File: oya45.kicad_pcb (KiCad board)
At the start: 2 copper layers, 190.5 x 95.2 mm, 94 parts, among them U1 ProMicro

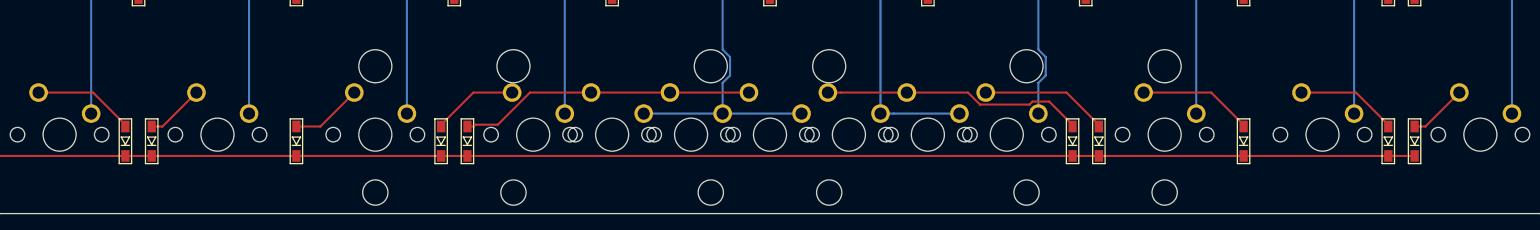
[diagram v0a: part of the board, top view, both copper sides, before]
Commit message: added bottom row footprints
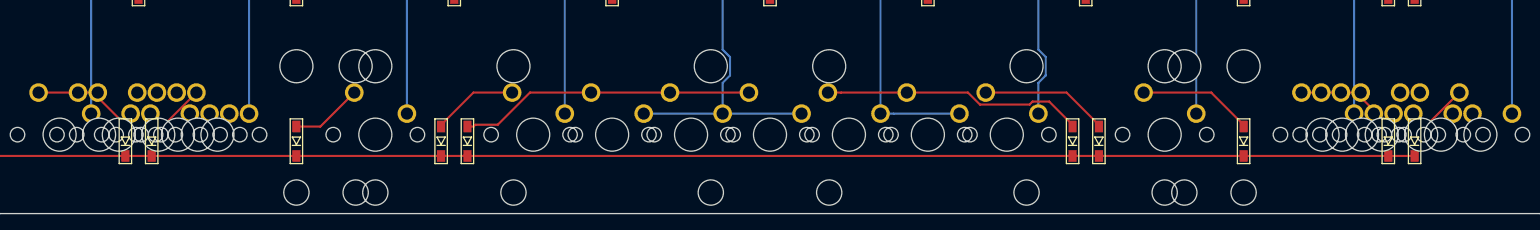
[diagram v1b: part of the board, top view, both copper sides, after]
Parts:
- added MX49: MX-NoLED, MX_Only:MXOnly-6.25U-ReversedStabilizers-NoSwitch, B.Cu at (142.9, 114.3)
- added MX50: MX-NoLED, MX_Only:MXOnly-7U-ReversedStabilizers-NoSwitch, B.Cu at (142.9, 114.3)
- added MX51: MX-NoLED, MX_Only:MXOnly-1.25U-NoLED, B.Cu at (73.8, 114.3)
- added MX52: MX-NoLED, MX_Only:MXOnly-1.25U-NoLED, B.Cu at (71.4, 114.3)
- added MX53: MX-NoLED, MX_Only:MXOnly-1.25U-NoLED, B.Cu at (64.3, 114.3)
- added MX54: MX-NoLED, MX_Only:MXOnly-1.5U-NoLED, B.Cu at (69.1, 114.3)
- added MX55: MX-NoLED, MX_Only:MXOnly-1.5U-NoLED, B.Cu at (61.9, 114.3)
- added MX57: MX-NoLED, MX_Only:MXOnly-1.25U-NoLED, B.Cu at (214.3, 114.3)
- added MX58: MX-NoLED, MX_Only:MXOnly-1.25U-NoLED, B.Cu at (211.9, 114.3)
- added MX59: MX-NoLED, MX_Only:MXOnly-1.25U-NoLED, B.Cu at (221.5, 114.3)
- added MX60: MX-NoLED, MX_Only:MXOnly-1.5U-NoLED, B.Cu at (216.7, 114.3)
- added MX61: MX-NoLED, MX_Only:MXOnly-1.5U-NoLED, B.Cu at (223.8, 114.3)

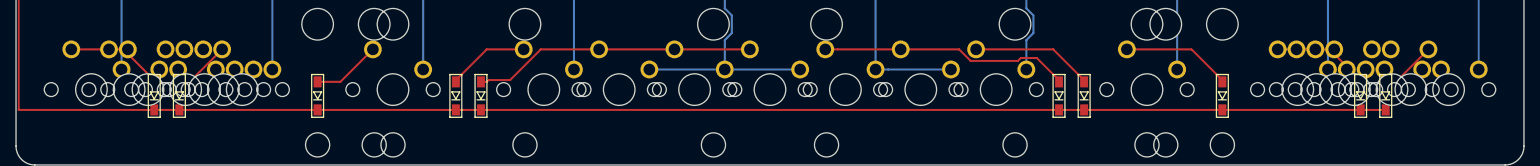
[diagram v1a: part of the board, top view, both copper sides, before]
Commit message: fixed diodes
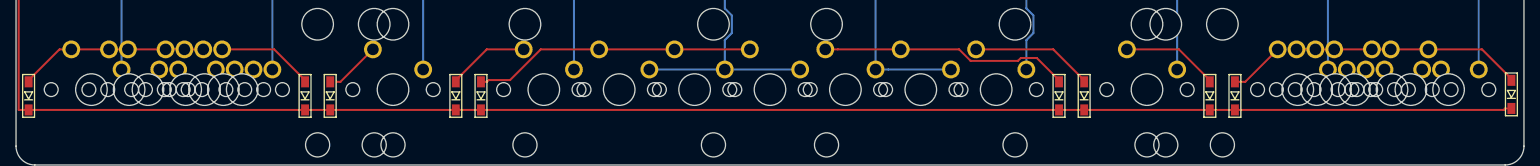
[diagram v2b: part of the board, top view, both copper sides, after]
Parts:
- moved D40 15.9 mm to (236.5, 114.9)
- moved D31 15.9 mm to (49.2, 115.1)
- moved D32 15.9 mm to (84.1, 115.1)
- moved D39 15.9 mm to (201.6, 115.1)
- moved D33 1.59 mm to (87.3, 115.1)
- moved D38 1.59 mm to (198.4, 115.1)
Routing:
- net Net-(D40-Pad2): track 7.10 -> 28.9 mm
- net row4: track 308.2 -> 324.1 mm
- net Net-(D31-Pad2): track 12.3 -> 23.9 mm
- net Net-(D39-Pad2): track 12.3 -> 7.10 mm
- net Net-(D32-Pad2): track 7.10 -> 12.3 mm
- net Net-(D33-Pad2): track 8.68 -> 6.30 mm
- net Net-(D38-Pad2): track 13.9 -> 12.3 mm
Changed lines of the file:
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@@
     (thickness 1.6)
     (drawings 8)
-    (tracks 241)
+    (tracks 244)
     (zones 0)
     (modules 106)
@@
   )
   (module kbd:D3_SMD_v2 (layer F.Cu)
-    (at 220.6625 115.09375 90)
+    (at 236.5375 114.90625 90)
     (descr "Resitance 3 pas")
     (tags R)
@@
   )
   (module kbd:D3_SMD_v2 (layer F.Cu)
-    (at 217.4875 115.09375 90)
+    (at 201.6125 115.09375 90)
     (descr "Resitance 3 pas")
     (tags R)
@@
   )
   (module kbd:D3_SMD_v2 (layer F.Cu)
-    (at 200.025 115.09375 90)
+    (at 198.4375 115.09375 90)
     (descr "Resitance 3 pas")
     (tags R)
@@
   )
   (module kbd:D3_SMD_v2 (layer F.Cu)
-    (at 85.725 115.09375 90)
+    (at 87.3125 115.09375 90)
     (descr "Resitance 3 pas")
     (tags R)
@@
   )
   (module kbd:D3_SMD_v2 (layer F.Cu)
-    (at 68.2625 115.09375 90)
+    (at 84.1375 115.09375 90)
     (descr "Resitance 3 pas")
     (tags R)
@@
       (effects (font (size 0.5 0.5) (thickness 0.125)))
     )
-    (fp_line (start -2.7 0.75) (end 2.7 0.75) (layer F.SilkS) (width 0.15))
-    (fp_line (start 2.7 -0.75) (end -2.7 -0.75) (layer F.SilkS) (width 0.15))
-    (fp_line (start -2.7 -0.75) (end -2.7 0.75) (layer F.SilkS) (width 0.15))
-    (fp_line (start 2.7 -0.75) (end 2.7 0.75) (layer F.SilkS) (width 0.15))
-    (fp_line (start 0.5 -0.5) (end 0.5 0.5) (layer F.SilkS) (width 0.15))
-    (fp_line (start 0.5 0.5) (end -0.4 0) (layer F.SilkS) (width 0.15))
-    (fp_line (start -0.4 0) (end 0.5 -0.5) (layer F.SilkS) (width 0.15))
     (fp_line (start -0.5 -0.5) (end -0.5 0.5) (layer F.SilkS) (width 0.15))
-    (pad 2 smd rect (at 1.775 0 90) (size 1.4 1) (layers F.Cu F.Paste F.Mask)
-      (net 36 "Net-(D32-Pad2)"))
+    (fp_line (start -0.4 0) (end 0.5 -0.5) (layer F.SilkS) (width 0.15))
+    (fp_line (start 0.5 0.5) (end -0.4 0) (layer F.SilkS) (width 0.15))
+    (fp_line (start 0.5 -0.5) (end 0.5 0.5) (layer F.SilkS) (width 0.15))
+    (fp_line (start 2.7 -0.75) (end 2.7 0.75) (layer F.SilkS) (width 0.15))
+    (fp_line (start -2.7 -0.75) (end -2.7 0.75) (layer F.SilkS) (width 0.15))
+    (fp_line (start 2.7 -0.75) (end -2.7 -0.75) (layer F.SilkS) (width 0.15))
+    (fp_line (start -2.7 0.75) (end 2.7 0.75) (layer F.SilkS) (width 0.15))
     (pad 1 smd rect (at -1.775 0 90) (size 1.4 1) (layers F.Cu F.Paste F.Mask)
       (net 34 row4))
+    (pad 2 smd rect (at 1.775 0 90) (size 1.4 1) (layers F.Cu F.Paste F.Mask)
+      (net 36 "Net-(D32-Pad2)"))
     (model ${KIGITHUB3D}/Diode_SMD.3dshapes/D_SOD-123.step
       (at (xyz 0 0 0))
@@
   )
   (module kbd:D3_SMD_v2 (layer F.Cu)
-    (at 65.0875 115.09375 90)
+    (at 49.2125 115.09375 90)
     (descr "Resitance 3 pas")
     (tags R)
@@
       (net 2 "Net-(D1-Pad2)"))
   )
+  (gr_line (start 47.625 121.44375) (end 47.625 30.95625) (layer Edge.Cuts) (width 0.05))
   (gr_arc (start 50.00625 121.44375) (end 47.625 121.44375) (angle -90) (layer Edge.Cuts) (width 0.05))
   (gr_arc (start 235.74375 121.44375) (end 235.74375 123.825) (angle -90) (layer Edge.Cuts) (width 0.05))
   (gr_arc (start 235.74375 30.95625) (end 238.125 30.95625) (angle -90) (layer Edge.Cuts) (width 0.05))
   (gr_arc (start 50.00625 30.95625) (end 50.00625 28.575) (angle -90) (layer Edge.Cuts) (width 0.05))
-  (gr_line (start 47.625 121.44375) (end 47.625 30.95625) (layer Edge.Cuts) (width 0.05))
   (gr_line (start 235.74375 123.825) (end 50.00625 123.825) (layer Edge.Cuts) (width 0.05))
   (gr_line (start 238.125 30.95625) (end 238.125 121.44375) (layer Edge.Cuts) (width 0.05))
@@
   (segment (start 226.06 71.12) (end 221.96125 75.21875) (width 0.254) (layer F.Cu) (net 22))
   (segment (start 113.39198 48.53302) (end 116.205 45.72) (width 0.254) (layer F.Cu) (net 23))
-  (segment (start 48.41875 48.53302) (end 113.39198 48.53302) (width 0.254) (layer F.Cu) (net 23))
   (segment (start 220.6625 97.81875) (end 48.41875 97.81875) (width 0.254) (layer F.Cu) (net 23))
+  (segment (start 48.41875 48.53302) (end 113.39198 48.53302) (width 0.254) (layer F.Cu) (net 23))
   (segment (start 48.41875 97.81875) (end 48.41875 48.53302) (width 0.254) (layer F.Cu) (net 23))
   (segment (start 66.675 94.06875) (end 66.675 94.26875) (width 0.254) (layer F.Cu) (net 24))
@@
   (segment (start 111.30599 48.07901) (end 113.665 45.72) (width 0.254) (layer F.Cu) (net 34))
   (segment (start 47.96474 48.07901) (end 111.30599 48.07901) (width 0.254) (layer F.Cu) (net 34))
-  (segment (start 47.96474 116.866139) (end 47.967351 116.86875) (width 0.254) (layer F.Cu) (net 34))
   (segment (start 47.96474 48.07901) (end 47.96474 116.866139) (width 0.254) (layer F.Cu) (net 34))
-  (segment (start 47.979621 116.86875) (end 47.97701 116.866139) (width 0.254) (layer F.Cu) (net 34))
-  (segment (start 220.6625 116.86875) (end 47.979621 116.86875) (width 0.254) (layer F.Cu) (net 34))
-  (segment (start 65.0875 113.11875) (end 65.0875 113.31875) (width 0.254) (layer F.Cu) (net 35))
-  (segment (start 61.18875 109.22) (end 65.0875 113.11875) (width 0.254) (layer F.Cu) (net 35))
-  (segment (start 54.61 109.22) (end 61.18875 109.22) (width 0.254) (layer F.Cu) (net 35))
-  (segment (start 69.56125 113.31875) (end 68.2625 113.31875) (width 0.254) (layer F.Cu) (net 36))
-  (segment (start 73.66 109.22) (end 69.56125 113.31875) (width 0.254) (layer F.Cu) (net 36))
-  (segment (start 88.61125 113.31875) (end 85.725 113.31875) (width 0.254) (layer F.Cu) (net 37))
+  (segment (start 47.96474 116.866139) (end 47.967351 116.86875) (width 0.254) (layer F.Cu) (net 34))
+  (segment (start 235.74375 116.68125) (end 236.5375 116.68125) (width 0.254) (layer F.Cu) (net 34))
+  (segment (start 235.55625 116.86875) (end 235.74375 116.68125) (width 0.254) (layer F.Cu) (net 34))
+  (segment (start 47.97701 116.866139) (end 47.979621 116.86875) (width 0.254) (layer F.Cu) (net 34))
+  (segment (start 47.979621 116.86875) (end 235.55625 116.86875) (width 0.254) (layer F.Cu) (net 34))
+  (segment (start 49.2125 113.11875) (end 49.2125 113.31875) (width 0.254) (layer F.Cu) (net 35))
+  (segment (start 53.11125 109.22) (end 49.2125 113.11875) (width 0.254) (layer F.Cu) (net 35))
+  (segment (start 71.27875 109.22) (end 53.11125 109.22) (width 0.254) (layer F.Cu) (net 35))
+  (segment (start 84.1375 113.11875) (end 84.1375 113.31875) (width 0.254) (layer F.Cu) (net 36))
+  (segment (start 80.23875 109.22) (end 84.1375 113.11875) (width 0.254) (layer F.Cu) (net 36))
+  (segment (start 73.66 109.22) (end 80.23875 109.22) (width 0.254) (layer F.Cu) (net 36))
+  (segment (start 88.61125 113.31875) (end 88.10625 113.31875) (width 0.254) (layer F.Cu) (net 37))
   (segment (start 92.71 109.22) (end 88.61125 113.31875) (width 0.254) (layer F.Cu) (net 37))
   (segment (start 103.1875 113.11875) (end 103.1875 113.31875) (width 0.254) (layer F.Cu) (net 38))
@@
   (segment (start 178.66375 109.22) (end 182.5625 113.11875) (width 0.254) (layer F.Cu) (net 41))
   (segment (start 168.91 109.22) (end 178.66375 109.22) (width 0.254) (layer F.Cu) (net 41))
-  (segment (start 200.025 113.11875) (end 200.025 113.31875) (width 0.254) (layer F.Cu) (net 42))
-  (segment (start 196.12625 109.22) (end 200.025 113.11875) (width 0.254) (layer F.Cu) (net 42))
-  (segment (start 187.96 109.22) (end 196.12625 109.22) (width 0.254) (layer F.Cu) (net 42))
-  (segment (start 217.4875 113.11875) (end 217.4875 113.31875) (width 0.254) (layer F.Cu) (net 43))
-  (segment (start 213.58875 109.22) (end 217.4875 113.11875) (width 0.254) (layer F.Cu) (net 43))
-  (segment (start 207.01 109.22) (end 213.58875 109.22) (width 0.254) (layer F.Cu) (net 43))
-  (segment (start 221.96125 113.31875) (end 220.6625 113.31875) (width 0.254) (layer F.Cu) (net 44))
-  (segment (start 226.06 109.22) (end 221.96125 113.31875) (width 0.254) (layer F.Cu) (net 44))
+  (segment (start 198.4375 113.11875) (end 198.4375 113.31875) (width 0.254) (layer F.Cu) (net 42))
+  (segment (start 194.53875 109.22) (end 198.4375 113.11875) (width 0.254) (layer F.Cu) (net 42))
+  (segment (start 187.96 109.22) (end 194.53875 109.22) (width 0.254) (layer F.Cu) (net 42))
+  (segment (start 202.91125 113.31875) (end 201.6125 113.31875) (width 0.254) (layer F.Cu) (net 43))
+  (segment (start 207.01 109.22) (end 202.91125 113.31875) (width 0.254) (layer F.Cu) (net 43))
+  (segment (start 236.5375 112.93125) (end 236.5375 113.13125) (width 0.254) (layer F.Cu) (net 44))
+  (segment (start 232.82625 109.22) (end 236.5375 112.93125) (width 0.254) (layer F.Cu) (net 44))
+  (segment (start 209.39125 109.22) (end 232.82625 109.22) (width 0.254) (layer F.Cu) (net 44))
   (segment (start 128.87625 40.66875) (end 123.825 45.72) (width 0.254) (layer F.Cu) (net 45))
   (segment (start 211.1375 40.66875) (end 128.87625 40.66875) (width 0.254) (layer F.Cu) (net 45))

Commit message: finished pcb
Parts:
- turned MX51 to 0 degrees
- turned MX58 to 0 degrees
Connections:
- MX51 pad 1: Net-(MX51-Pad1) -> col0
- MX52 pad 1: Net-(MX52-Pad1) -> col0
- MX53 pad 1: Net-(MX53-Pad1) -> col0
- MX54 pad 1: Net-(MX54-Pad1) -> col0
- MX55 pad 1: Net-(MX55-Pad1) -> col0
- MX57 pad 1: Net-(MX57-Pad1) -> col9
- MX58 pad 1: Net-(MX58-Pad1) -> col9
- MX59 pad 1: Net-(MX59-Pad1) -> col9
- MX60 pad 1: Net-(MX60-Pad1) -> col9
- MX61 pad 1: Net-(MX61-Pad1) -> col9
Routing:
- net col9: track 175.0 -> 216.9 mm
- net col0: track 126.2 -> 165.2 mm
- net Net-(D31-Pad2): track 23.9 -> 51.3 mm
- net Net-(D40-Pad2): track 28.9 -> 51.3 mm
- net row4: track 324.1 -> 330.8 mm
- net Net-(D33-Pad2): track 6.30 -> 7.10 mm

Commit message: finished pcb
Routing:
- net col7: track 142.6 -> 143.3 mm
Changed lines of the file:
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@@
     (thickness 1.6)
     (drawings 8)
-    (tracks 277)
+    (tracks 281)
     (zones 0)
     (modules 106)
@@
   (segment (start 84.8915 116.86875) (end 87.3125 116.86875) (width 0.254) (layer F.Cu) (net 34))
   (segment (start 84.1375 116.86875) (end 84.8915 116.86875) (width 0.254) (layer F.Cu) (net 34))
-  (segment (start 83.3835 116.86875) (end 84.1375 116.86875) (width 0.254) (layer F.Cu) (net 34))
-  (segment (start 79.420249 120.832001) (end 83.3835 116.86875) (width 0.254) (layer F.Cu) (net 34))
-  (segment (start 53.929751 120.832001) (end 79.420249 120.832001) (width 0.254) (layer F.Cu) (net 34))
-  (segment (start 49.9665 116.86875) (end 53.929751 120.832001) (width 0.254) (layer F.Cu) (net 34))
-  (segment (start 49.2125 116.86875) (end 49.9665 116.86875) (width 0.254) (layer F.Cu) (net 34))
+  (segment (start 200.8585 116.86875) (end 87.3125 116.86875) (width 0.254) (layer F.Cu) (net 34))
+  (segment (start 201.6125 116.86875) (end 200.8585 116.86875) (width 0.254) (layer F.Cu) (net 34))
   (segment (start 202.3665 116.86875) (end 201.6125 116.86875) (width 0.254) (layer F.Cu) (net 34))
   (segment (start 206.329751 120.832001) (end 202.3665 116.86875) (width 0.254) (layer F.Cu) (net 34))
   (segment (start 232.586749 120.832001) (end 206.329751 120.832001) (width 0.254) (layer F.Cu) (net 34))
-  (segment (start 236.5375 116.88125) (end 232.586749 120.832001) (width 0.254) (layer F.Cu) (net 34))
   (segment (start 236.5375 116.68125) (end 236.5375 116.88125) (width 0.254) (layer F.Cu) (net 34))
-  (segment (start 200.8585 116.86875) (end 87.3125 116.86875) (width 0.254) (layer F.Cu) (net 34))
-  (segment (start 201.6125 116.86875) (end 200.8585 116.86875) (width 0.254) (layer F.Cu) (net 34))
+  (segment (start 236.5375 116.88125) (end 232.586749 120.832001) (width 0.254) (layer F.Cu) (net 34))
+  (segment (start 49.2125 116.86875) (end 49.9665 116.86875) (width 0.254) (layer F.Cu) (net 34))
+  (segment (start 49.9665 116.86875) (end 53.929751 120.832001) (width 0.254) (layer F.Cu) (net 34))
+  (segment (start 83.3835 116.86875) (end 84.1375 116.86875) (width 0.254) (layer F.Cu) (net 34))
+  (segment (start 79.420249 120.832001) (end 83.3835 116.86875) (width 0.254) (layer F.Cu) (net 34))
+  (segment (start 53.929751 120.832001) (end 79.420249 120.832001) (width 0.254) (layer F.Cu) (net 34))
   (segment (start 49.2125 113.11875) (end 49.2125 113.31875) (width 0.254) (layer F.Cu) (net 35))
   (segment (start 53.11125 109.22) (end 49.2125 113.11875) (width 0.254) (layer F.Cu) (net 35))
@@
   (segment (start 232.82625 109.22) (end 236.5375 112.93125) (width 0.254) (layer F.Cu) (net 44))
   (segment (start 211.7725 109.22) (end 232.82625 109.22) (width 0.254) (layer F.Cu) (net 44))
+  (segment (start 214.47125 119.38) (end 230.48875 119.38) (width 0.254) (layer F.Cu) (net 44))
   (segment (start 236.5375 113.33125) (end 236.5375 113.13125) (width 0.254) (layer F.Cu) (net 44))
   (segment (start 230.48875 119.38) (end 236.5375 113.33125) (width 0.254) (layer F.Cu) (net 44))
-  (segment (start 214.47125 119.38) (end 230.48875 119.38) (width 0.254) (layer F.Cu) (net 44))
   (segment (start 128.87625 40.66875) (end 123.825 45.72) (width 0.254) (layer F.Cu) (net 45))
   (segment (start 211.1375 40.66875) (end 128.87625 40.66875) (width 0.254) (layer F.Cu) (net 45))
@@
   (segment (start 165.735 35.56) (end 160.45177 30.27677) (width 0.254) (layer B.Cu) (net 57))
   (segment (start 160.45177 30.27677) (end 134.713249 30.27677) (width 0.254) (layer B.Cu) (net 57))
-  (segment (start 194.31 54.61) (end 194.31 111.76) (width 0.254) (layer B.Cu) (net 58))
   (segment (start 184.785 45.085) (end 184.785 35.56) (width 0.254) (layer B.Cu) (net 58))
   (segment (start 194.31 54.61) (end 184.785 45.085) (width 0.254) (layer B.Cu) (net 58))
@@
   (segment (start 184.785 35.56) (end 179.04776 29.82276) (width 0.254) (layer B.Cu) (net 58))
   (segment (start 179.04776 29.82276) (end 134.525192 29.82276) (width 0.254) (layer B.Cu) (net 58))
+  (segment (start 194.31 104.045166) (end 195.195801 104.930967) (width 0.254) (layer B.Cu) (net 58))
+  (segment (start 194.31 54.61) (end 194.31 104.045166) (width 0.254) (layer B.Cu) (net 58))
+  (segment (start 195.195801 104.930967) (end 195.195801 107.159033) (width 0.254) (layer B.Cu) (net 58))
+  (segment (start 194.31 108.044834) (end 194.31 111.76) (width 0.254) (layer B.Cu) (net 58))
+  (segment (start 195.195801 107.159033) (end 194.31 108.044834) (width 0.254) (layer B.Cu) (net 58))
   (segment (start 213.36 54.61) (end 213.36 111.76) (width 0.254) (layer B.Cu) (net 59))
   (segment (start 203.835 45.085) (end 203.835 35.56) (width 0.254) (layer B.Cu) (net 59))
